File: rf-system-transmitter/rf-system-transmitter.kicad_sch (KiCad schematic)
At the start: 52 parts, among them IC1 nRF905, IC2 MCP1700T-3302E_TT, J1 Battery input, J2 CONREVSMA001-G, J3 SWD, SW1 SW_Push, U1 STM32F103C8Tx, X1 16MHZ, X2 16MHZ

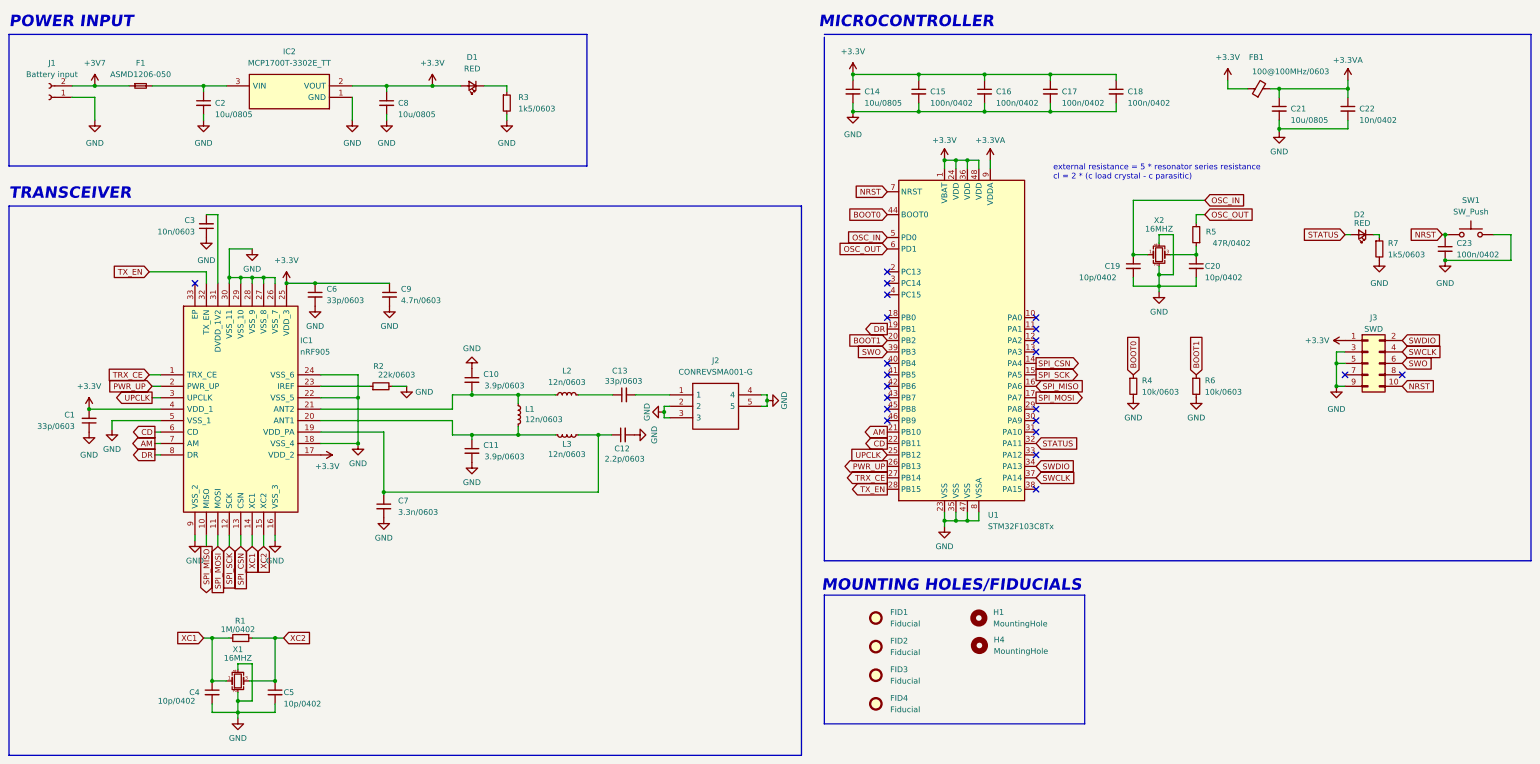
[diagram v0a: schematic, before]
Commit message: adding LCSC Part # and small PCB modifs
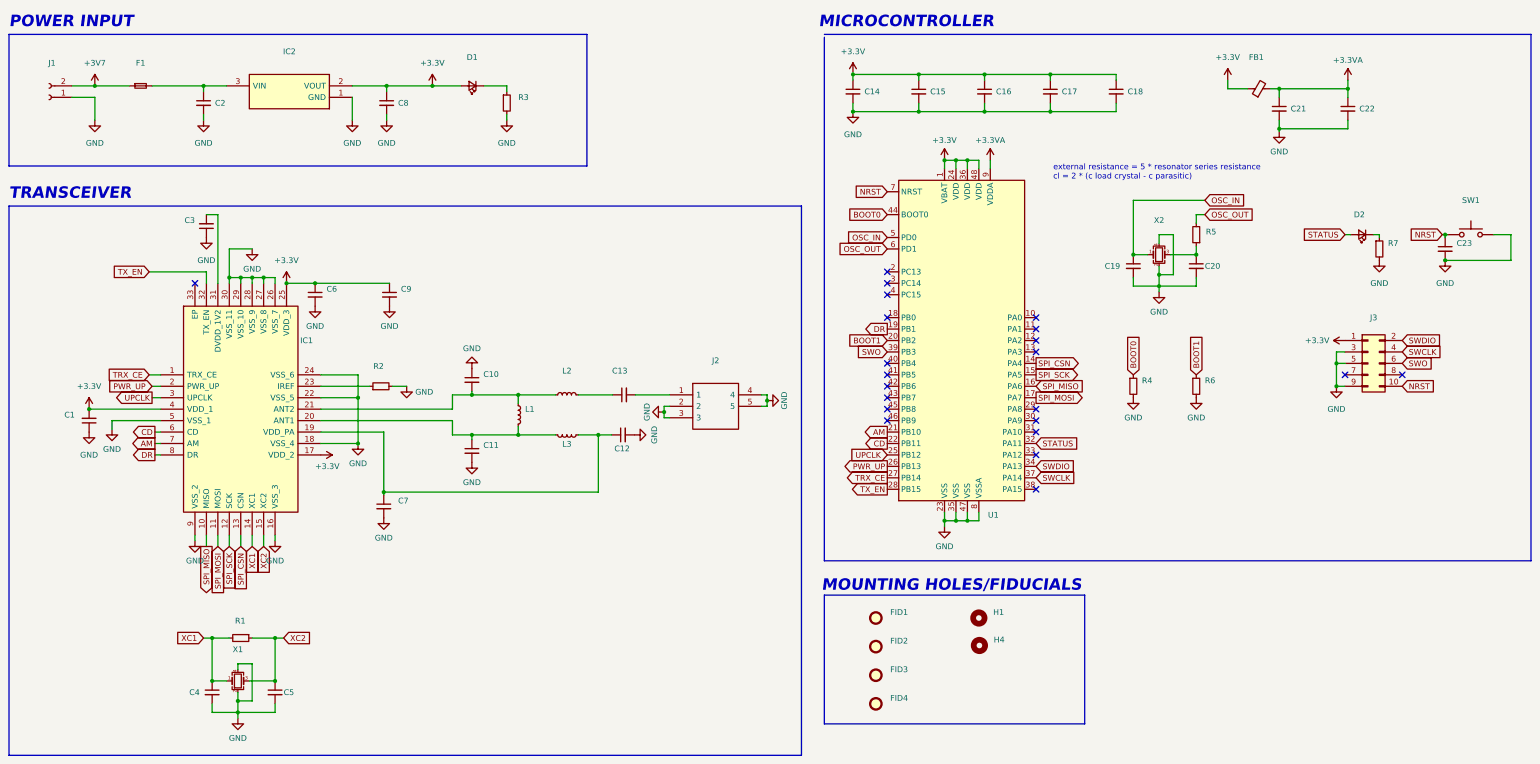
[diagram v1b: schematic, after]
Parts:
- C1, C13, C6: value 33p/0603 -> (none); footprint Capacitor_SMD:C_0603_1608Metric -> (none); LCSC Part # (none) -> C1663
- C10, C11: value 3.9p/0603 -> (none); footprint Capacitor_SMD:C_0603_1608Metric -> (none); LCSC Part # (none) -> C123566
- C12: value 2.2p/0603 -> (none); footprint Capacitor_SMD:C_0603_1608Metric -> (none); LCSC Part # (none) -> C1663
- C14, C2, C21, C8: value 10u/0805 -> (none); footprint Capacitor_SMD:C_0805_2012Metric -> (none); LCSC Part # (none) -> C440198
- C15, C16, C17, C18, C23: value 100n/0402 -> (none); footprint Capacitor_SMD:C_0402_1005Metric -> (none); LCSC Part # (none) -> C307331
- C19, C20, C4, C5: value 10p/0402 -> (none); footprint Capacitor_SMD:C_0402_1005Metric -> (none); LCSC Part # (none) -> C32949
- C22: value 10n/0402 -> (none); footprint Capacitor_SMD:C_0402_1005Metric -> (none); LCSC Part # (none) -> C15195
- C3: value 10n/0603 -> (none); footprint Capacitor_SMD:C_0603_1608Metric -> (none); LCSC Part # (none) -> C57112
- C7: value 3.3n/0603 -> (none); footprint Capacitor_SMD:C_0603_1608Metric -> (none); LCSC Part # (none) -> C1613
- C9: value 4.7n/0603 -> (none); footprint Capacitor_SMD:C_0603_1608Metric -> (none); LCSC Part # (none) -> C53987
- D1, D2: value RED -> (none); footprint LED_SMD:LED_0603_1608Metric -> (none)
- F1: value ASMD1206-050 -> (none); footprint Fuse:Fuse_1206_3216Metric -> (none); LCSC Part # (none) -> C135338
- FB1: value 100@100MHz/0603 -> (none); footprint Inductor_SMD:L_0603_1608Metric -> (none); LCSC Part # (none) -> C1002
- FID1, FID2, FID3, FID4: value Fiducial -> (none); footprint Fiducial:Fiducial_1mm_Mask2mm -> (none)
- H1, H4: value MountingHole -> (none); footprint MountingHole:MountingHole_3.2mm_M3 -> (none)
- IC1: value nRF905 -> (none); footprint nrf905:nrf905 -> (none)
- IC2: value MCP1700T-3302E_TT -> (none); footprint MCP1700T-3302E_TT:MCP1700T-3302E_TT -> (none)
- J1: value Battery input -> (none); footprint Connector_JST:JST_PH_B2B-PH-K_1x02_P2.00mm_Vertical -> (none); LCSC Part # (none) -> C131337
- J2: value CONREVSMA001-G -> (none); footprint CONREVSMA001:CONREVSMA001G -> (none)
- J3: value SWD -> (none); footprint Connector_PinHeader_2.54mm:PinHeader_2x05_P2.54mm_Vertical_SMD -> (none); LCSC Part # (none) -> C780052
- L1, L2, L3: value 12n/0603 -> (none); footprint Inductor_SMD:L_0603_1608Metric -> (none)
- R1: value 1M/0402 -> (none); footprint Resistor_SMD:R_0402_1005Metric -> (none)
- R2: value 22k/0603 -> (none); footprint Resistor_SMD:R_0603_1608Metric -> (none)
- R3, R7: value 1k5/0603 -> (none); footprint Resistor_SMD:R_0603_1608Metric -> (none)
- R4, R6: value 10k/0603 -> (none); footprint Resistor_SMD:R_0603_1608Metric -> (none)
- R5: value 47R/0402 -> (none); footprint Resistor_SMD:R_0402_1005Metric -> (none)
- SW1: value SW_Push -> (none); footprint Button_Switch_THT:SW_PUSH_6mm -> (none)
- U1: value STM32F103C8Tx -> (none); footprint Package_QFP:LQFP-48_7x7mm_P0.5mm -> (none)
- X1, X2: value 16MHZ -> (none); footprint Crystal:Crystal_SMD_3225-4Pin_3.2x2.5mm -> (none); LCSC Part # (none) -> C112972
